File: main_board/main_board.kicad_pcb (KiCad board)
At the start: 2 copper layers, 8 parts, among them U1 LT1722CS5-TRMPBF, U2 TS5A4624DCKR, U3 AD5160, U4 TS5A4624DCKR, U5 AD8031ARTZ-REEL7, U6 LT1722CS5-TRMPBF, U7 LTC2315CTS8-12-PBF, U8 LT1818IS5-TRMPBF

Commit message: tweaks
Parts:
- added U10: ~, Cmod_S7:Cmod_S7, F.Cu at (198.8, 68.5)

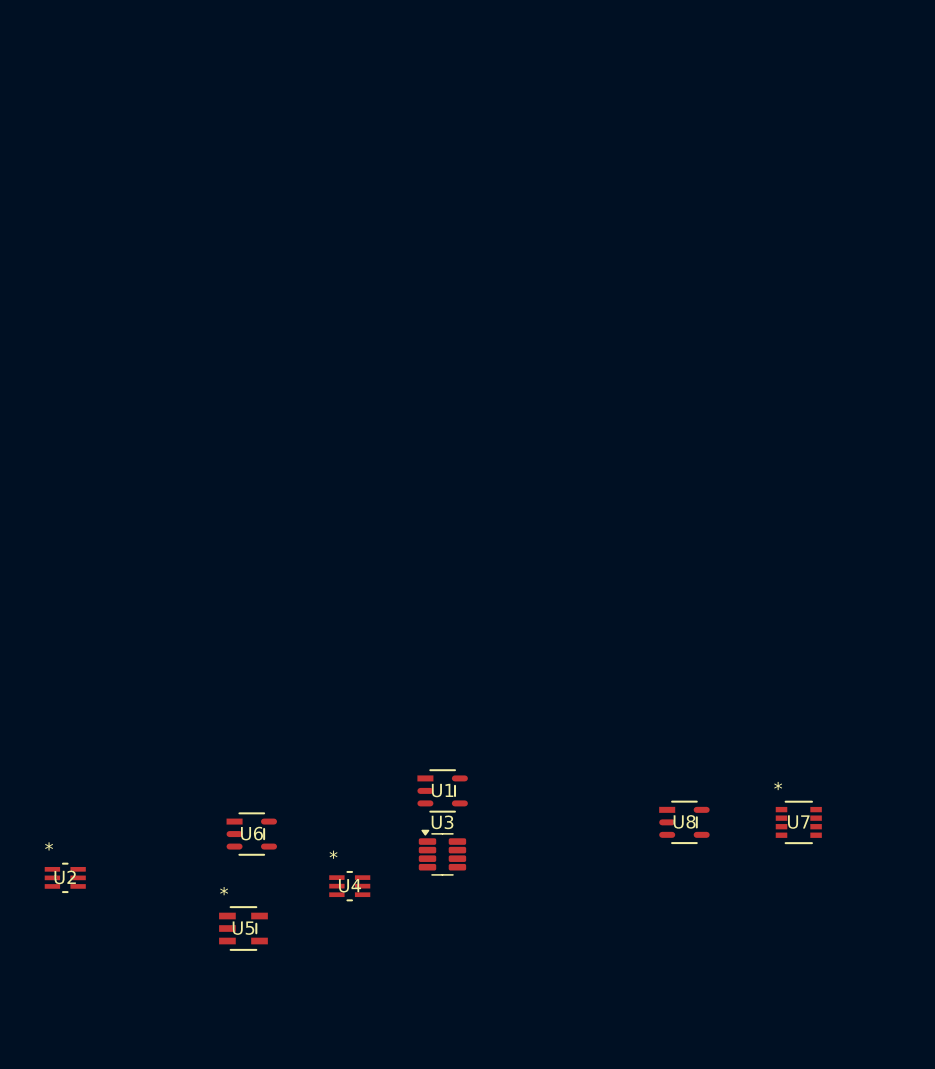
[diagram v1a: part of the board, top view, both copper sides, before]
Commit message: Added PCBway drc ruleset, connected mux IO, ADC SPI interface, Pot SPI interface & 0603 footprints to all passive devices.
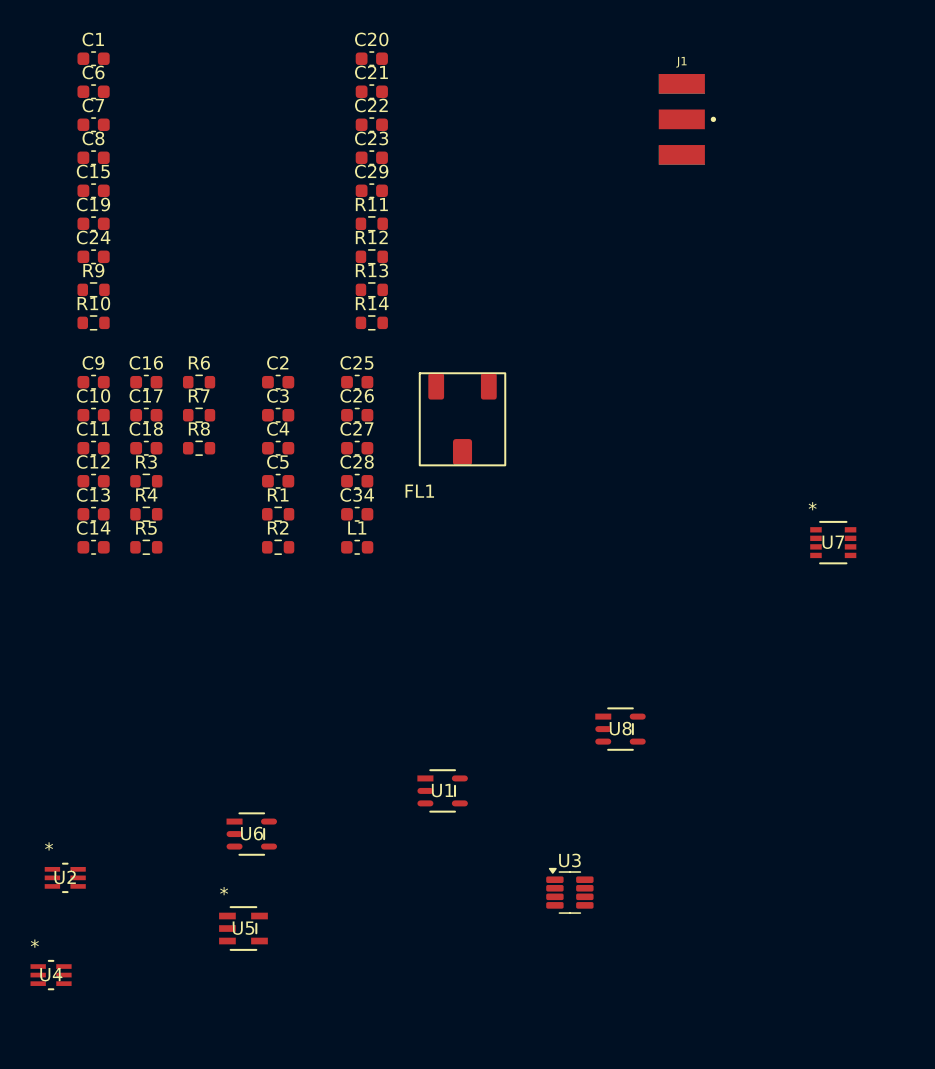
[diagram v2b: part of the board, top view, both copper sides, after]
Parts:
- added C1: 1u, Capacitor_SMD:C_0603_1608Metric, F.Cu at (126.7, 63.9)
- added C10: 100n, Capacitor_SMD:C_0603_1608Metric, F.Cu at (126.7, 91.0)
- added C11: 10u, Capacitor_SMD:C_0603_1608Metric, F.Cu at (126.7, 93.5)
- added C12: 100n, Capacitor_SMD:C_0603_1608Metric, F.Cu at (126.7, 96.0)
- added C13: 36p, Capacitor_SMD:C_0603_1608Metric, F.Cu at (126.7, 98.5)
- added C14: 36p, Capacitor_SMD:C_0603_1608Metric, F.Cu at (126.7, 101.0)
- added C15: 100n, Capacitor_SMD:C_0603_1608Metric, F.Cu at (126.7, 73.9)
- added C16: 100n, Capacitor_SMD:C_0603_1608Metric, F.Cu at (130.7, 88.5)
- added C17: 1u, Capacitor_SMD:C_0603_1608Metric, F.Cu at (130.7, 91.0)
- added C18: 100n, Capacitor_SMD:C_0603_1608Metric, F.Cu at (130.7, 93.5)
- added C19: 100n, Capacitor_SMD:C_0603_1608Metric, F.Cu at (126.7, 76.4)
- added C2: 100n, Capacitor_SMD:C_0603_1608Metric, F.Cu at (140.7, 88.5)
- added C20: 4.7u, Capacitor_SMD:C_0603_1608Metric, F.Cu at (147.8, 63.9)
- added C21: 4.7u, Capacitor_SMD:C_0603_1608Metric, F.Cu at (147.8, 66.4)
- added C22: 4.7u, Capacitor_SMD:C_0603_1608Metric, F.Cu at (147.8, 68.9)
- added C23: 47p, Capacitor_SMD:C_0603_1608Metric, F.Cu at (147.8, 71.4)
- added C24: C, Capacitor_SMD:C_0603_1608Metric, F.Cu at (126.7, 79.0)
- added C25: 10u, Capacitor_SMD:C_0603_1608Metric, F.Cu at (146.7, 88.5)
- added C26: 100n, Capacitor_SMD:C_0603_1608Metric, F.Cu at (146.7, 91.0)
- added C27: 22u, Capacitor_SMD:C_0603_1608Metric, F.Cu at (146.7, 93.5)
- added C28: 22u, Capacitor_SMD:C_0603_1608Metric, F.Cu at (146.7, 96.0)
- added C29: 100n, Capacitor_SMD:C_0603_1608Metric, F.Cu at (147.8, 73.9)
- added C3: 1u, Capacitor_SMD:C_0603_1608Metric, F.Cu at (140.7, 91.0)
- added C34: 1u, Capacitor_SMD:C_0603_1608Metric, F.Cu at (146.7, 98.5)
- added C4: 100n, Capacitor_SMD:C_0603_1608Metric, F.Cu at (140.7, 93.5)
- added C5: ~, Capacitor_SMD:C_0603_1608Metric, F.Cu at (140.7, 96.0)
- added C6: C, Capacitor_SMD:C_0603_1608Metric, F.Cu at (126.7, 66.4)
- added C7: C, Capacitor_SMD:C_0603_1608Metric, F.Cu at (126.7, 68.9)
- added C8: C, Capacitor_SMD:C_0603_1608Metric, F.Cu at (126.7, 71.4)
- added C9: 10u, Capacitor_SMD:C_0603_1608Metric, F.Cu at (126.7, 88.5)
- added FL1: ~, 457k_bp_filter_fp:457k_bandpass_FL, F.Cu at (151.4, 94.8)
- added J1: CON-SMA-EDGE-S, SMA_male_fp:RFSOLUTIONS_CON-SMA-EDGE-S, F.Cu at (171.4, 68.5)
- added L1: 4.7u, Inductor_SMD:L_0603_1608Metric, F.Cu at (146.7, 101.0)
- added R1: 100k, Resistor_SMD:R_0603_1608Metric, F.Cu at (140.7, 98.5)
- added R10: 10k, Resistor_SMD:R_0603_1608Metric, F.Cu at (126.7, 84.0)
- added R11: 50, Resistor_SMD:R_0603_1608Metric, F.Cu at (147.8, 76.4)
- added R12: 3k, Resistor_SMD:R_0603_1608Metric, F.Cu at (147.8, 79.0)
- added R13: 2k, Resistor_SMD:R_0603_1608Metric, F.Cu at (147.8, 81.5)
- added R14: 33, Resistor_SMD:R_0603_1608Metric, F.Cu at (147.8, 84.0)
- added R2: 100k, Resistor_SMD:R_0603_1608Metric, F.Cu at (140.7, 101.0)
- added R3: 4.99k, Resistor_SMD:R_0603_1608Metric, F.Cu at (130.7, 96.0)
- added R4: 10k, Resistor_SMD:R_0603_1608Metric, F.Cu at (130.7, 98.5)
- added R5: 10k, Resistor_SMD:R_0603_1608Metric, F.Cu at (130.7, 101.0)
- added R6: 174k, Resistor_SMD:R_0603_1608Metric, F.Cu at (134.7, 88.5)
- added R7: 866, Resistor_SMD:R_0603_1608Metric, F.Cu at (134.7, 91.0)
- added R8: 1.33k, Resistor_SMD:R_0603_1608Metric, F.Cu at (134.7, 93.5)
- added R9: 10k, Resistor_SMD:R_0603_1608Metric, F.Cu at (126.7, 81.5)
- moved U4 23.7 mm to (123.4, 133.6)
- moved U7 21.4 mm to (182.9, 100.7)
- moved U3 10.1 mm to (162.9, 127.3)
- moved U8 8.60 mm to (166.7, 114.9)
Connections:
- U10 pad 1: unconnected-(U10-Pad1) -> /Bypass_sig
- U10 pad 2: unconnected-(U10-Pad2) -> /Pot_CLK
- U10 pad 24: unconnected-(U10-Pad24) -> +5V
- U10 pad 25: unconnected-(U10-Pad25) -> GND
- U10 pad 3: unconnected-(U10-Pad3) -> /Pot_CS
- U10 pad 44: unconnected-(U10-Pad44) -> /Serial_Data_Out
- U10 pad 47: unconnected-(U10-Pad47) -> /SCK
- U10 pad 48: unconnected-(U10-Pad48) -> /CS_bar
- U10 pad 6: unconnected-(U10-Pad6) -> /Pot_SDI
- U3 pad 4: /PGA/Pot_CLK -> /Pot_CLK
- U3 pad 5: /PGA/Pot_SDI -> /Pot_SDI
- U3 pad 6: /PGA/Pot_CS -> /Pot_CS

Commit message: add 1u cap on input to 3.3v reg
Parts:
- C5: value ~ -> 2u
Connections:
- U7 pad 5: /ADC/IO_Interface_Digital_Power -> +3.3V
- U7 pad 6: /ADC/Serial_Data_Out -> Net-(U7-SDO)
- U7 pad 7: /ADC/SCK -> /SCK
- U7 pad 8: /ADC/CS_bar -> /CS_bar
- U8 pad 1: Net-(D1-A) -> Net-(U8--IN)
- U8 pad 4: Net-(D1-A) -> Net-(U8--IN)

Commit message: Finalized last schematic changes, awaing group approval.
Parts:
- added C30: 1u, Capacitor_SMD:C_0603_1608Metric, F.Cu at (100.6, 121.4)
- added U12: MIC5365-3.3YC5-TR, linear_regulator_fp:SC-70_C5_MCH-M, F.Cu at (96.1, 122.5)
- added U9: AP63205WU-7, step_down_converter:SOIC_05WU-7_DIO-M, F.Cu at (96.5, 117.6)
- C5: value 2u -> .2u

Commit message: update todos
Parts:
- C24: value C -> 22n
- C6: value C -> .15u
- C7, C8: value C -> 68p
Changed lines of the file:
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@@
 			(psa4output no)
 			(plot_black_and_white yes)
-			(plotinvisibletext no)
 			(sketchpadsonfab no)
 			(plotpadnumbers no)
@@
 			)
 		)
-		(property "Datasheet" ""
+		(property "Datasheet" "~"
 			(at 0 0 0)
 			(unlocked yes)
@@
 			)
 		)
-		(property "Datasheet" ""
+		(property "Datasheet" "~"
 			(at 0 0 0)
 			(unlocked yes)
@@
 			)
 		)
-		(property "Datasheet" ""
+		(property "Datasheet" "~"
 			(at 0 0 0)
 			(unlocked yes)
@@
 			)
 		)
-		(property "Datasheet" ""
+		(property "Datasheet" "~"
 			(at 0 0 0)
 			(unlocked yes)
@@
 			)
 		)
-		(property "Datasheet" ""
+		(property "Datasheet" "~"
 			(at 0 0 0)
 			(unlocked yes)
@@
 			)
 		)
-		(property "Datasheet" ""
+		(property "Datasheet" "~"
 			(at 0 0 0)
 			(unlocked yes)
@@
 			)
 		)
-		(property "Datasheet" ""
+		(property "Datasheet" "~"
 			(at 0 0 0)
 			(unlocked yes)
@@
 			)
 		)
-		(property "Datasheet" ""
+		(property "Datasheet" "~"
 			(at 0 0 0)
 			(unlocked yes)
@@
 			)
 		)
-		(fp_text user "${REFERENCE}"
-			(at 0 0 0)
-			(unlocked yes)
+		(fp_text user "*"
+			(at -1.2319 -2.1486 0)
 			(layer "F.Fab")
 			(effects
@@
 			)
 		)
-		(fp_text user "*"
-			(at -1.2319 -2.1486 0)
+		(fp_text user "${REFERENCE}"
+			(at 0 0 0)
+			(unlocked yes)
 			(layer "F.Fab")
 			(effects
@@
 			)
 		)
-		(property "Datasheet" ""
+		(property "Datasheet" "~"
 			(at 0 0 0)
 			(unlocked yes)
@@
 			)
 		)
-		(property "Datasheet" ""
+		(property "Datasheet" "~"
 			(at 0 0 0)
 			(unlocked yes)
@@
 			)
 		)
-		(property "Datasheet" ""
+		(property "Datasheet" "~"
 			(at 0 0 0)
 			(unlocked yes)
@@
 			)
 		)
-		(property "Datasheet" ""
+		(property "Datasheet" "~"
 			(at 0 0 0)
 			(unlocked yes)
@@
 			)
 		)
-		(property "Datasheet" ""
+		(property "Datasheet" "~"
 			(at 0 0 0)
 			(unlocked yes)
@@
 			)
 		)
-		(property "Datasheet" ""
+		(property "Datasheet" "~"
 			(at 0 0 0)
 			(unlocked yes)
@@
 			)
 		)
-		(property "Datasheet" ""
+		(property "Datasheet" "~"
 			(at 0 0 0)
 			(unlocked yes)
@@
 			)
 		)
-		(property "Datasheet" ""
+		(property "Datasheet" "~"
 			(at 0 0 0)
 			(unlocked yes)
@@
 			)
 		)
-		(property "Datasheet" ""
+		(property "Datasheet" "~"
 			(at 0 0 0)
 			(unlocked yes)
@@
 			)
 		)
-		(property "Datasheet" ""
+		(property "Datasheet" "~"
 			(at 0 0 0)
 			(unlocked yes)
@@
 			)
 		)
-		(property "Datasheet" ""
+		(property "Datasheet" "~"
 			(at 0 0 0)
 			(unlocked yes)
@@
 			)
 		)
-		(property "Datasheet" ""
+		(property "Datasheet" "~"
 			(at 0 0 0)
 			(unlocked yes)
@@
 			)
 		)
-		(property "Datasheet" ""
+		(property "Datasheet" "~"
 			(at 0 0 0)
 			(unlocked yes)
@@
 			)
 		)
-		(property "Value" "C"
+		(property "Value" ".15u"
 			(at 0 1.43 0)
 			(layer "F.Fab")
@@
 			)
 		)
-		(property "Datasheet" ""
+		(property "Datasheet" "~"
 			(at 0 0 0)
 			(unlocked yes)
@@
 			)
 		)
-		(property "Value" "C"
+		(property "Value" "22n"
 			(at 0 1.43 0)
 			(layer "F.Fab")
@@
 			)
 		)
-		(property "Datasheet" ""
+		(property "Datasheet" "~"
 			(at 0 0 0)
 			(unlocked yes)
@@
 			)
 		)
-		(property "Datasheet" ""
+		(property "Datasheet" "~"
 			(at 0 0 0)
 			(unlocked yes)
@@
 			)
 		)
-		(property "Datasheet" ""
+		(property "Datasheet" "~"
 			(at 0 0 0)
 			(unlocked yes)
@@
 			)
 		)
-		(property "Datasheet" ""
+		(property "Datasheet" "~"
 			(at 0 0 0)
 			(unlocked yes)
@@
 			)
 		)
-		(property "Value" "C"
+		(property "Value" "68p"
 			(at 0 1.43 0)
 			(layer "F.Fab")
@@
 			)
 		)
-		(property "Datasheet" ""
+		(property "Datasheet" "~"
 			(at 0 0 0)
 			(unlocked yes)
@@
 			)
 		)
-		(property "Datasheet" ""
+		(property "Datasheet" "~"
 			(at 0 0 0)
 			(unlocked yes)
@@
 			)
 		)
-		(property "Datasheet" ""
+		(property "Datasheet" "~"
 			(at 0 0 0)
 			(unlocked yes)
@@
 			)
 		)
-		(property "Datasheet" ""
+		(property "Datasheet" "~"
 			(at 0 0 0)
 			(unlocked yes)
@@
 			)
 		)
-		(property "Datasheet" ""
+		(property "Datasheet" "~"
 			(at 0 0 0)
 			(unlocked yes)
@@
 			)
 		)
-		(property "Datasheet" ""
+		(property "Datasheet" "~"
 			(at 0 0 0)
 			(unlocked yes)
@@
 			)
 		)
-		(property "Datasheet" ""
+		(property "Datasheet" "~"
 			(at 0 0 0)
 			(unlocked yes)
@@
 			)
 		)
-		(property "Datasheet" ""
+		(property "Datasheet" "~"
 			(at 0 0 0)
 			(unlocked yes)
@@
 			)
 		)
-		(property "Datasheet" ""
+		(property "Datasheet" "~"
 			(at 0 0 0)
 			(unlocked yes)
@@
 			)
 		)
-		(property "Value" "C"
+		(property "Value" "68p"
 			(at 0 1.43 0)
 			(layer "F.Fab")
@@
 			)
 		)
-		(property "Datasheet" ""
+		(property "Datasheet" "~"
 			(at 0 0 0)
 			(unlocked yes)
@@
 			)
 		)
-		(property "Datasheet" ""
+		(property "Datasheet" "~"
 			(at 0 0 0)
 			(unlocked yes)
@@
 			)
 		)
-		(property "Datasheet" ""
+		(property "Datasheet" "~"
 			(at 0 0 0)
 			(unlocked yes)
@@
 			)
 		)
-		(property "Datasheet" ""
+		(property "Datasheet" "~"
 			(at 0 0 0)
 			(unlocked yes)
@@
 			)
 		)
-		(property "Datasheet" ""
+		(property "Datasheet" "~"
 			(at 0 0 0)
 			(unlocked yes)
@@
 			)
 		)
-		(property "Datasheet" ""
+		(property "Datasheet" "~"
 			(at 0 0 0)
 			(unlocked yes)
@@
 			)
 		)
-		(property "Datasheet" ""
+		(property "Datasheet" "~"
 			(at 0 0 0)
 			(unlocked yes)
@@
 			)
 		)
-		(property "Datasheet" ""
+		(property "Datasheet" "~"
 			(at 0 0 0)
 			(unlocked yes)
@@
 			)
 		)
-		(property "Datasheet" ""
+		(property "Datasheet" "~"
 			(at 0 0 0)
 			(unlocked yes)
@@
 		(fp_text user "*"
 			(at -1.4732 -2.601 0)
-			(unlocked yes)
 			(layer "F.SilkS")
 			(effects
@@
 		(fp_text user "*"
 			(at -1.4732 -2.601 0)
+			(unlocked yes)
 			(layer "F.SilkS")
 			(effects
@@
 		(fp_text user "*"
 			(at -0.5969 -1.6358 0)
+			(unlocked yes)
 			(layer "F.Fab")
 			(effects
@@
 			)
 		)
-		(fp_text user "*"
-			(at -0.5969 -1.6358 0)
+		(fp_text user "${REFERENCE}"
+			(at 0 0 0)
 			(unlocked yes)
 			(layer "F.Fab")
@@
 			)
 		)
-		(fp_text user "${REFERENCE}"
-			(at 0 0 0)
-			(unlocked yes)
+		(fp_text user "*"
+			(at -0.5969 -1.6358 0)
 			(layer "F.Fab")
 			(effects
@@
 			)
 		)
-		(property "Datasheet" ""
+		(property "Datasheet" "~"
 			(at 0 0 0)
 			(unlocked yes)
@@
 			)
 		)
-		(fp_text user "*"
-			(at -1.2319 -2.1486 0)
+		(fp_text user "${REFERENCE}"
+			(at 0 0 0)
 			(unlocked yes)
 			(layer "F.Fab")
@@
 			)
 		)
-		(fp_text user "${REFERENCE}"
-			(at 0 0 0)
-			(unlocked yes)
+		(fp_text user "*"
+			(at -1.2319 -2.1486 0)
 			(layer "F.Fab")
 			(effects
@@
 		(fp_text user "*"
 			(at -1.2319 -2.1486 0)
+			(unlocked yes)
 			(layer "F.Fab")
 			(effects
@@
 			)
 		)
-		(property "Datasheet" ""
+		(property "Datasheet" "~"
 			(at 0 0 0)
 			(unlocked yes)

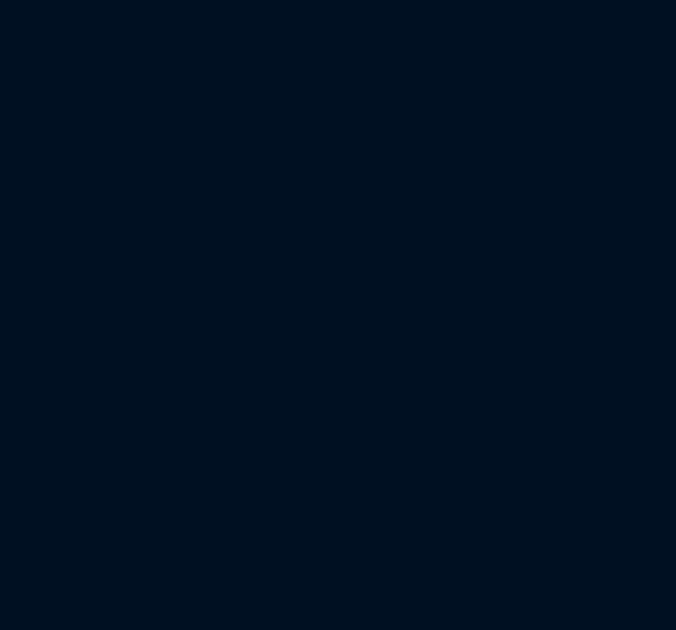
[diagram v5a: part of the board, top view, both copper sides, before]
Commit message: added power headers.
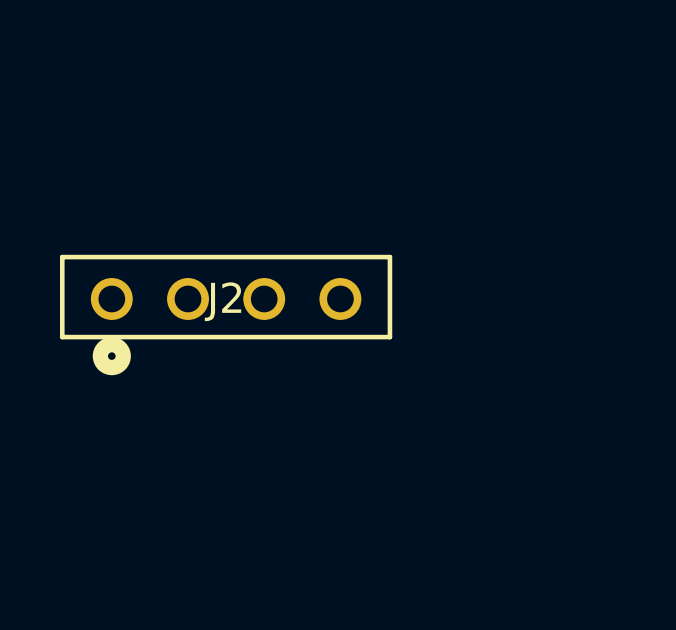
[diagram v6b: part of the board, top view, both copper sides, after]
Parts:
- added J2: TSW-104-14-F-S, pin_header_fp:CON4_1X4_TU_TSW, F.Cu at (98.2, 95.4)

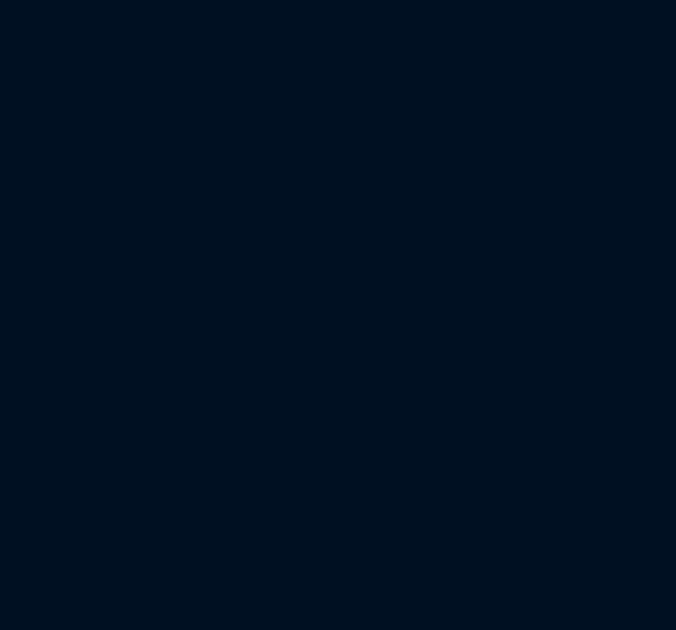
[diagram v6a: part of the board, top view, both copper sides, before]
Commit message: added pin for uart.
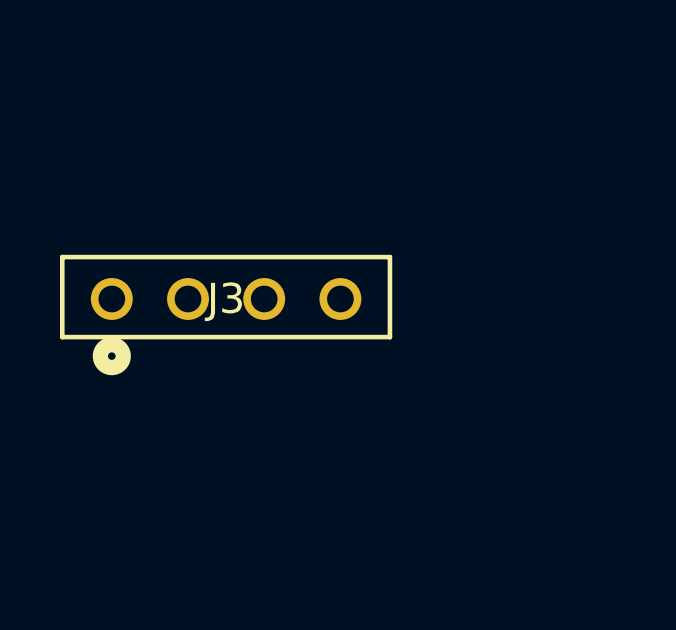
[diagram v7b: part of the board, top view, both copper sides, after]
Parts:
- added J3: TSW-104-14-F-S, pin_header_fp:CON4_1X4_TU_TSW, F.Cu at (97.1, 80.1)
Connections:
- U10 pad 1: /Bypass_sig -> /Bypass_ctrl
- U10 pad 9: unconnected-(U10-Pad9) -> /uart
